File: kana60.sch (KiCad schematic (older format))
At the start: 135 parts, among them SW1 SW_PUSH, SW10 SW_PUSH, SW11 SW_PUSH, SW12 SW_PUSH, SW13 SW_PUSH, SW14 SW_PUSH, SW15 SW_PUSH, SW16 SW_PUSH, SW17 SW_PUSH, SW18 SW_PUSH, SW19 SW_PUSH, SW2 SW_PUSH, SW20 SW_PUSH, SW21 SW_PUSH, SW22 SW_PUSH, SW23 SW_PUSH, SW24 SW_PUSH, SW25 SW_PUSH, SW26 SW_PUSH, SW27 SW_PUSH, SW28 SW_PUSH, SW29 SW_PUSH, SW3 SW_PUSH, SW30 SW_PUSH, SW31 SW_PUSH, SW32 SW_PUSH, SW33 SW_PUSH, SW34 SW_PUSH, SW35 SW_PUSH, SW36 SW_PUSH, SW37 SW_PUSH, SW38 SW_PUSH, SW39 SW_PUSH, SW4 SW_PUSH, SW40 SW_PUSH, SW41 SW_PUSH, SW42 SW_PUSH, SW43 SW_PUSH, SW44 SW_PUSH, SW45 SW_PUSH, SW46 SW_PUSH, SW47 SW_PUSH, SW48 SW_PUSH, SW49 SW_PUSH, SW5 SW_PUSH, SW50 SW_PUSH, SW51 SW_PUSH, SW52 SW_PUSH, SW53 SW_PUSH, SW54 SW_PUSH, SW55 SW_PUSH, SW56 SW_PUSH, SW57 SW_PUSH, SW58 SW_PUSH, SW59 SW_PUSH, SW6 SW_PUSH, SW60 SW_PUSH, SW61 SW_PUSH, SW62 SW_PUSH, SW63 SW_PUSH, SW64 SW_PUSH, SW65 SW_PUSH, SW66 SW_PUSH, SW67 SW_PUSH, SW68 SW_PUSH, SW7 SW_PUSH, SW8 SW_PUSH, SW9 SW_PUSH, U1 ProMicro

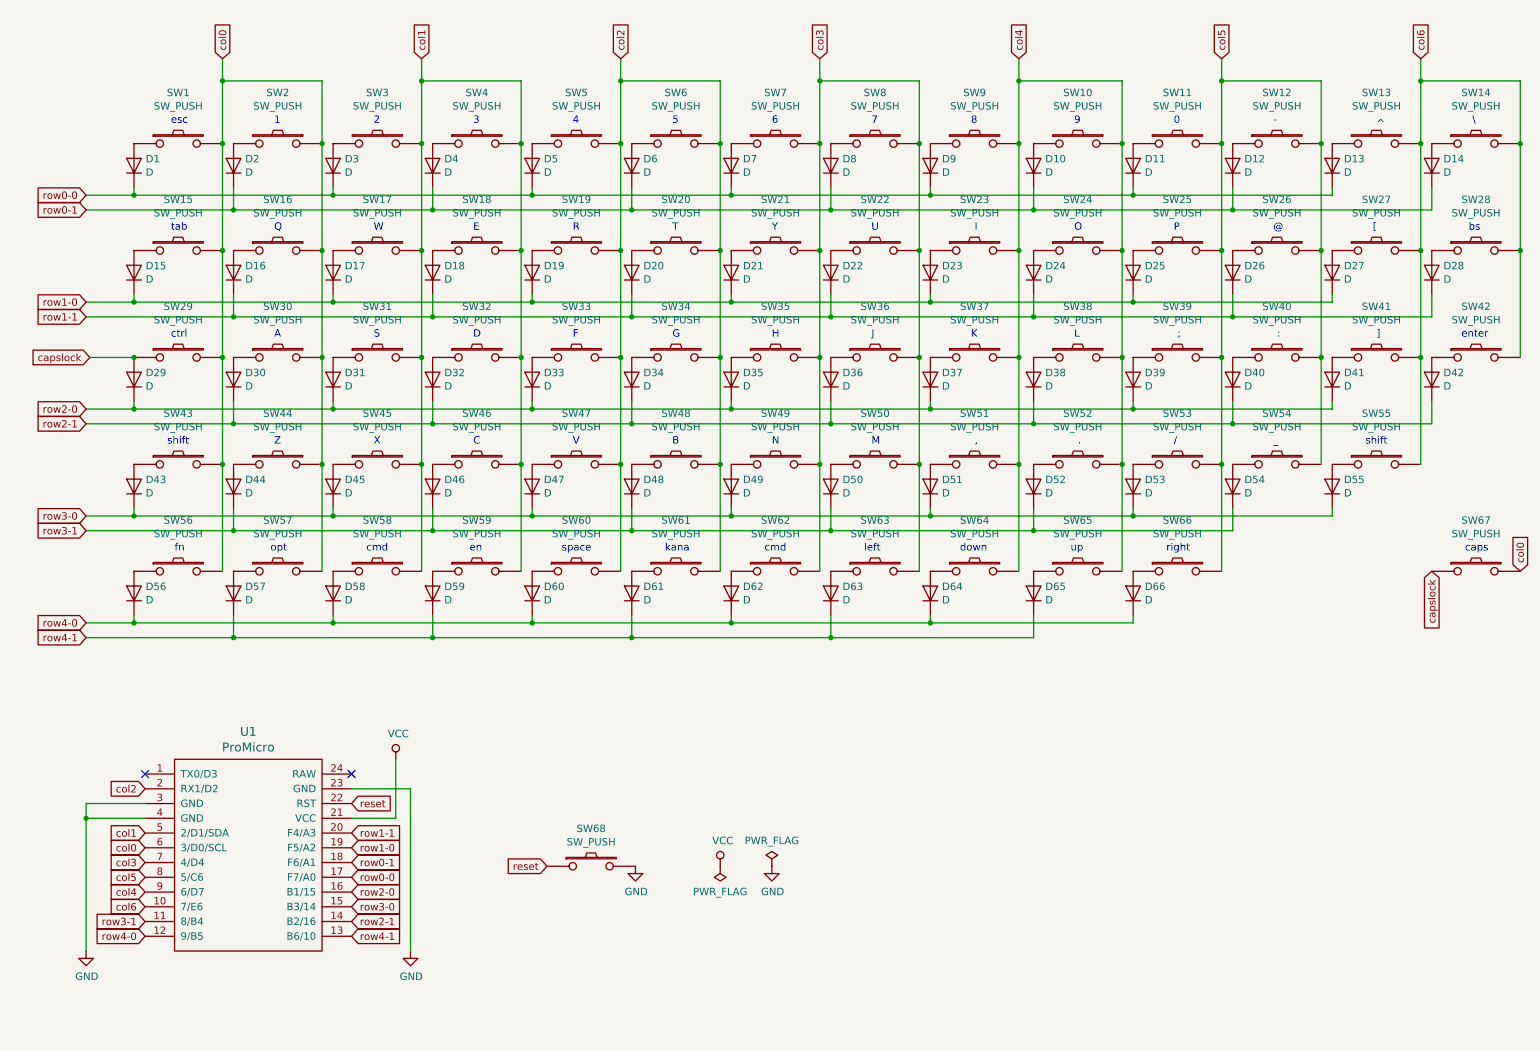
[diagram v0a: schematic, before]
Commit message: update schematic
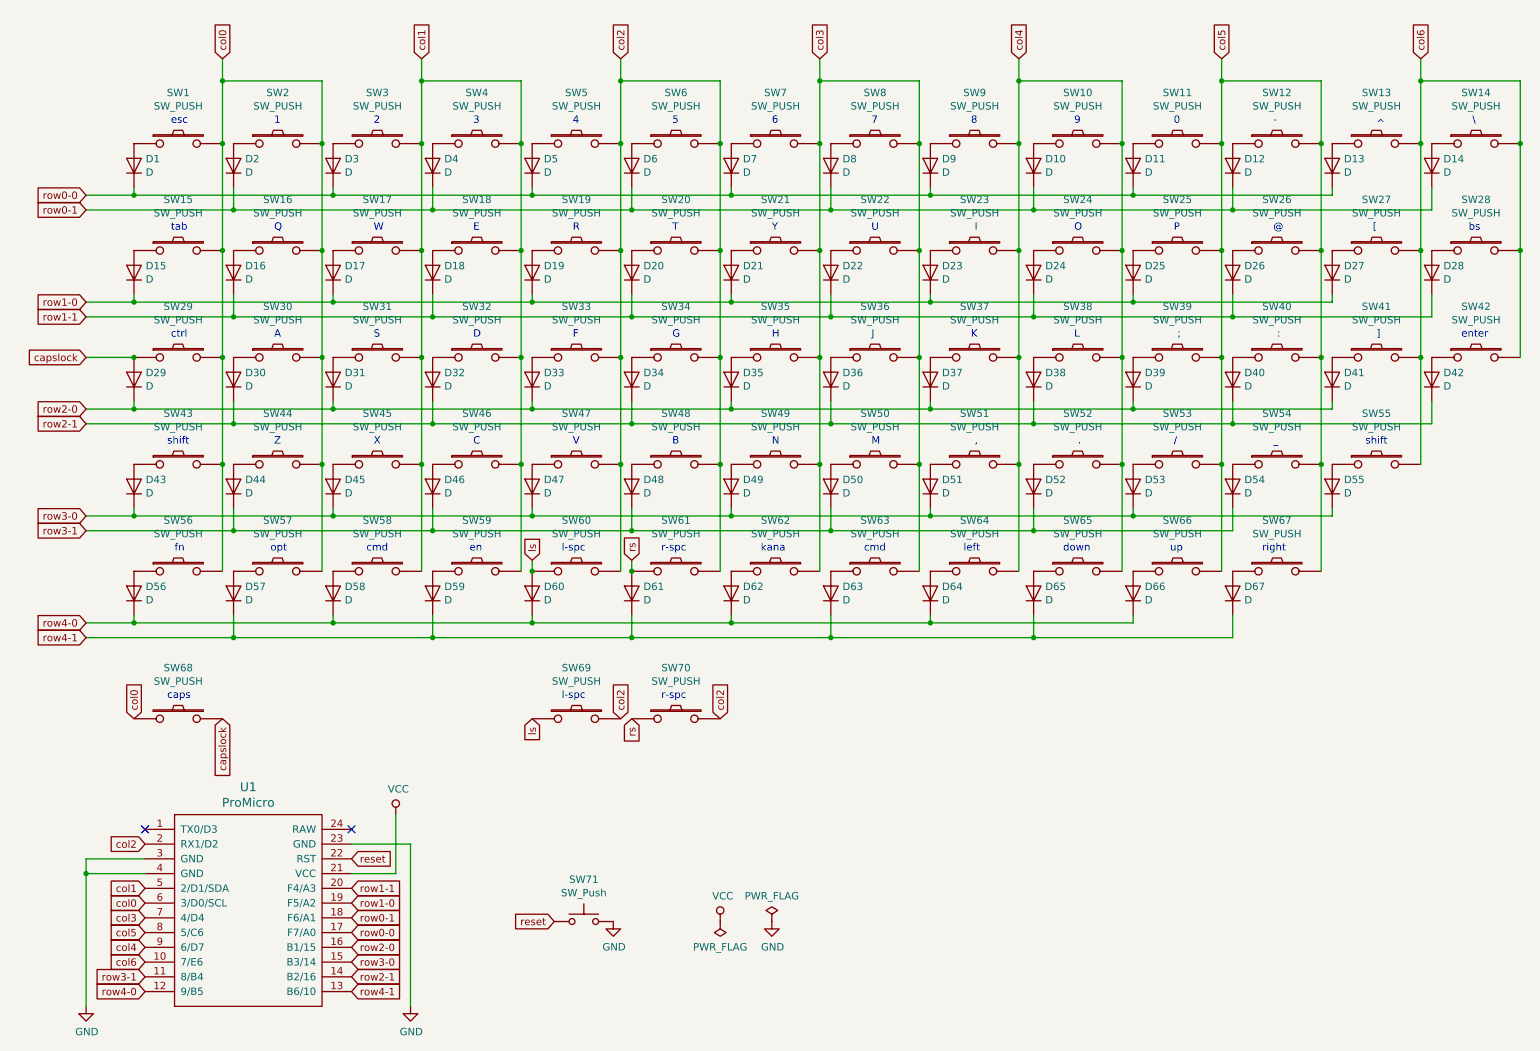
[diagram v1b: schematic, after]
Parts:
- removed SW68: SW_PUSH, kbd:ResetSW_1side, symbol kbd:SW_PUSH
- added D67: D, Keebio-Parts:Diode-dual, symbol Device:D
- added SW67, SW69: SW_PUSH, Keebio-Parts:MX-Alps-Choc-1U-NoLED, symbol kbd:SW_PUSH
- added SW70: SW_PUSH, kana60:MX-Alps-Choc-2U-NoLED, symbol kbd:SW_PUSH
- added SW71: SW_Push, kbd:ResetSW, symbol Switch:SW_Push
- SW42, SW43, SW60: footprint Keebio-Parts:MX-Alps-Choc-1U-NoLED -> kana60:MX-Alps-Choc-2U-NoLED
- renumbered SW67 to SW68
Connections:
- net GND: now also SW71.2
- net capslock: now also SW68.2; no longer SW68.1
- net col0: now also SW68.1; no longer SW68.2
- net col2: now also SW69.2, SW70.2
- net col5: now also SW67.2
- net reset: now also SW71.1
- net row4-1: now also D67.1 (K)
- net ls: now reaches D60.2 (A), SW60.1
- net ls: now also SW69.1
- net rs: now reaches D61.2 (A), SW61.1
- net rs: now also SW70.1
- new net: D67.2 (A), SW67.1
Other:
- note added: "l-spc"
- note added: "r-spc"
- note removed: "space"
- moved on the sheet: SW68, U1

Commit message: update footprint
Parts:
- SW1, SW10, SW11, SW12, SW13, SW14, SW16, SW17, SW18, SW19, SW2, SW20, SW21, SW22, SW23, SW24, SW25, SW26, SW27, SW28, SW3, SW30, SW31, SW32, SW33, SW34, SW35, SW36, SW37, SW38, SW39, SW4, SW40, SW41, SW44, SW45, SW46, SW47, SW48, SW49, SW5, SW50, SW51, SW52, SW53, SW54, SW6, SW61, SW64, SW65, SW66, SW67, SW68, SW69, SW7, SW8, SW9: footprint Keebio-Parts:MX-Alps-Choc-1U-NoLED -> Keebio-Parts:Hybrid_PCB_100H
- SW15: footprint Keebio-Parts:MX-Alps-Choc-1U-NoLED -> Keebio-Parts:Hybrid_PCB_150H
- SW29, SW55: footprint Keebio-Parts:MX-Alps-Choc-1U-NoLED -> Keebio-Parts:Hybrid_PCB_175H
- SW42, SW43, SW60, SW70: footprint kana60:MX-Alps-Choc-2U-NoLED -> Keebio-Parts:Hybrid_PCB_200H
- SW56, SW57, SW58, SW59, SW62, SW63: footprint Keebio-Parts:MX-Alps-Choc-1U-NoLED -> Keebio-Parts:Hybrid_PCB_125H
